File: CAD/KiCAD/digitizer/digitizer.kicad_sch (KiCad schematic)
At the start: 0 parts

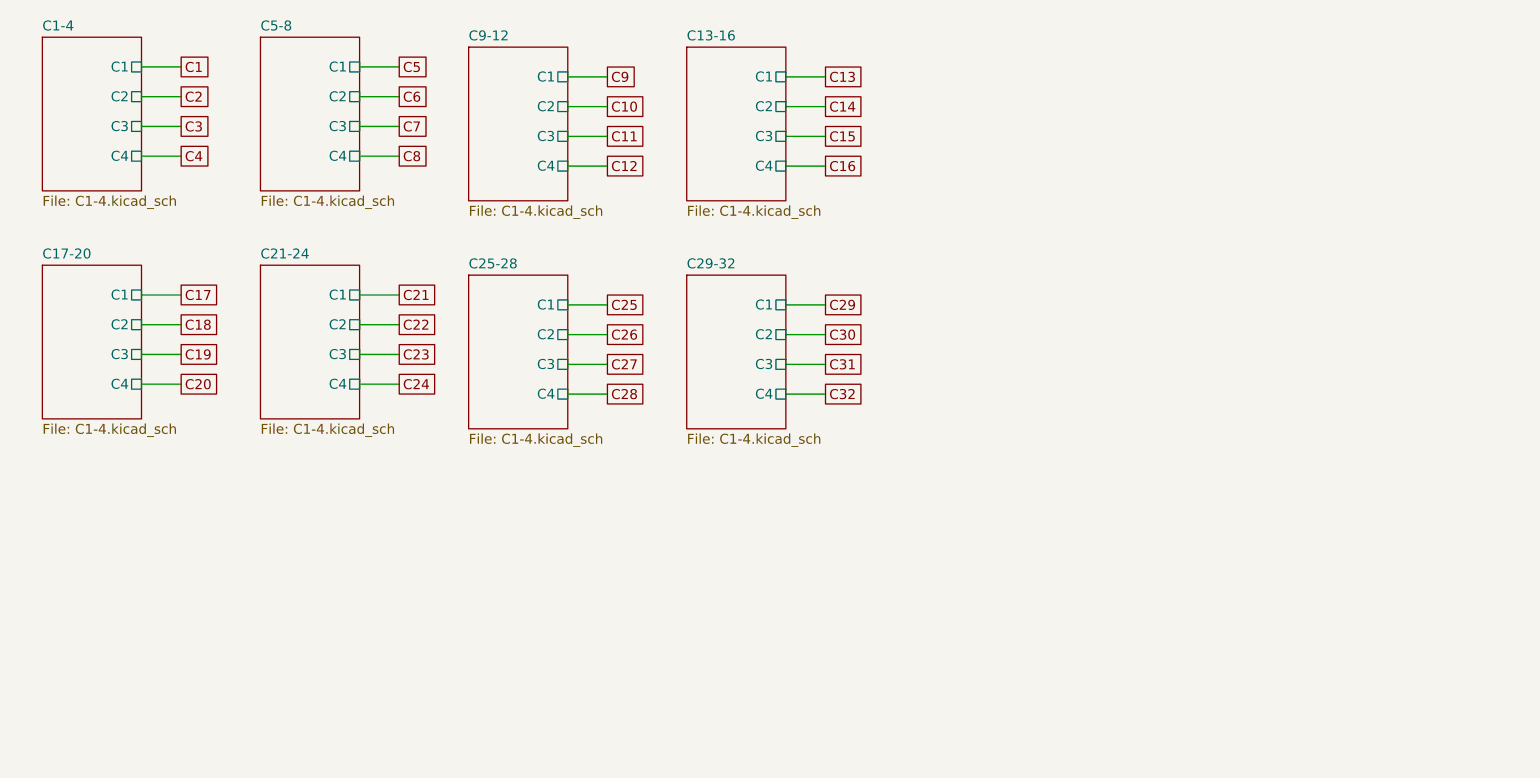
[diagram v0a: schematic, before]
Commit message: add MCP23017 for rows (no routing)
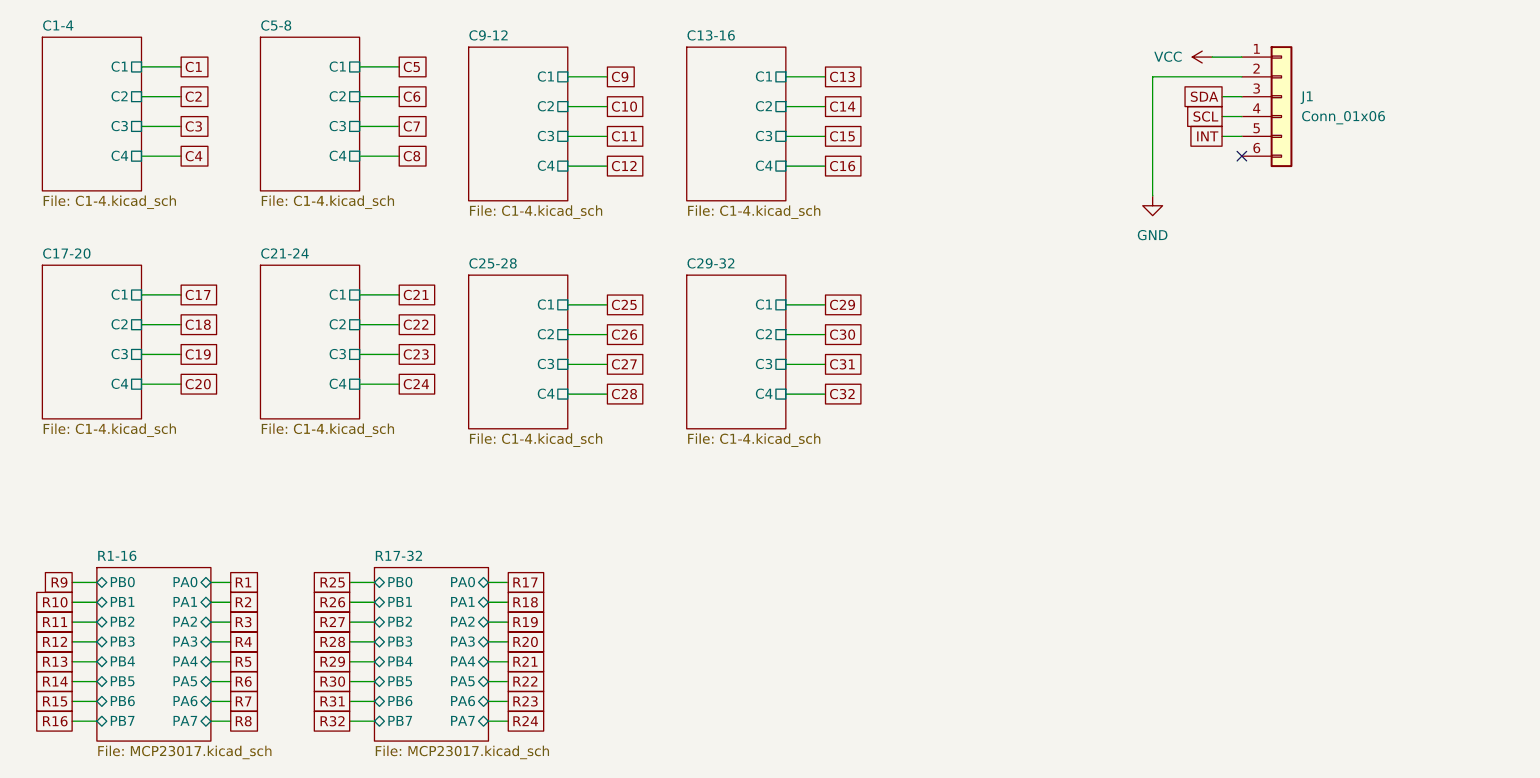
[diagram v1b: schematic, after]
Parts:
- added J1: Conn_01x06, Connector_PinHeader_2.54mm:PinHeader_1x06_P2.54mm_Vertical, symbol Connector_Generic:Conn_01x06
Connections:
- new net GND: J1.2 (Pin_2)
- new net INT: J1.5 (Pin_5)
- new net SCL: J1.4 (Pin_4)
- new net SDA: J1.3 (Pin_3)
- new net VCC: J1.1 (Pin_1)
- no-connect marks 0 -> 1
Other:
- added sheet R1-16 (MCP23017.kicad_sch)
- added sheet R17-32 (MCP23017.kicad_sch)

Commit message: one MCP23017 added and routed
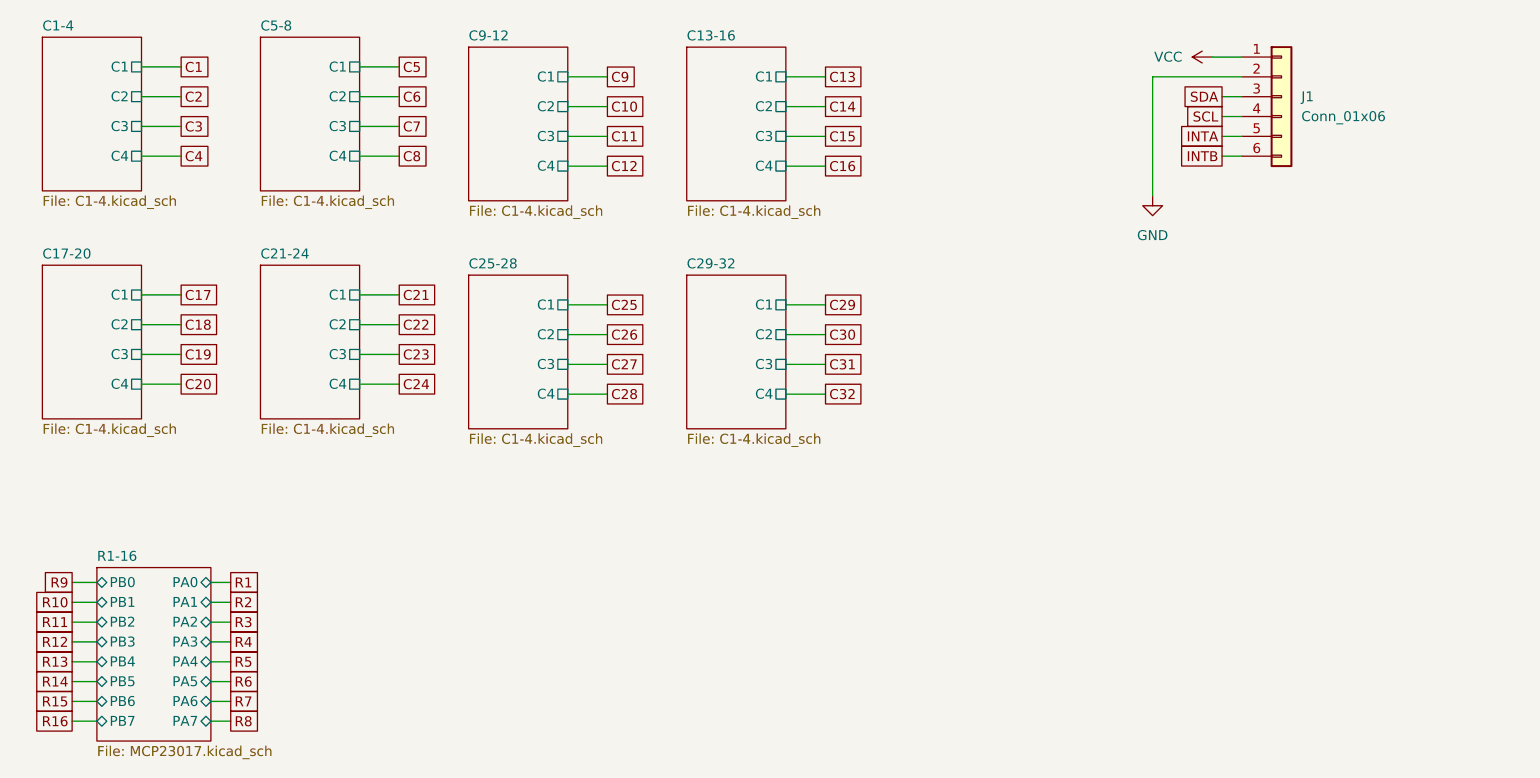
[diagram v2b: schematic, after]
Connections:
- net INTB: now reaches J1.6 (Pin_6)
- net INT renamed INTA
- no-connect marks 1 -> 0
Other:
- removed sheet R17-32

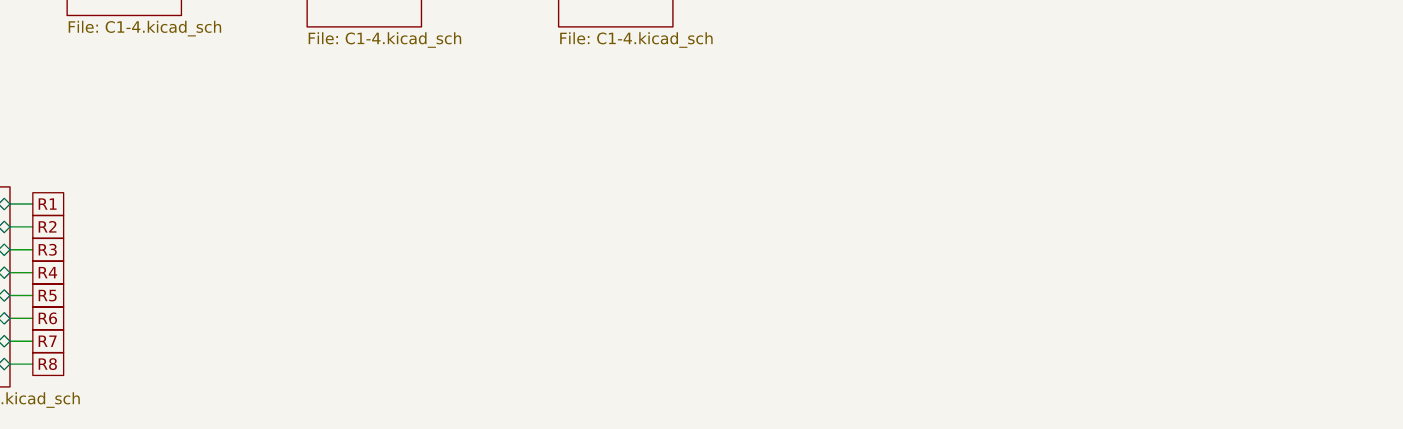
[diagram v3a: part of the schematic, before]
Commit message: digitizer draft with MCP23017 routing
Made-with: Cursor
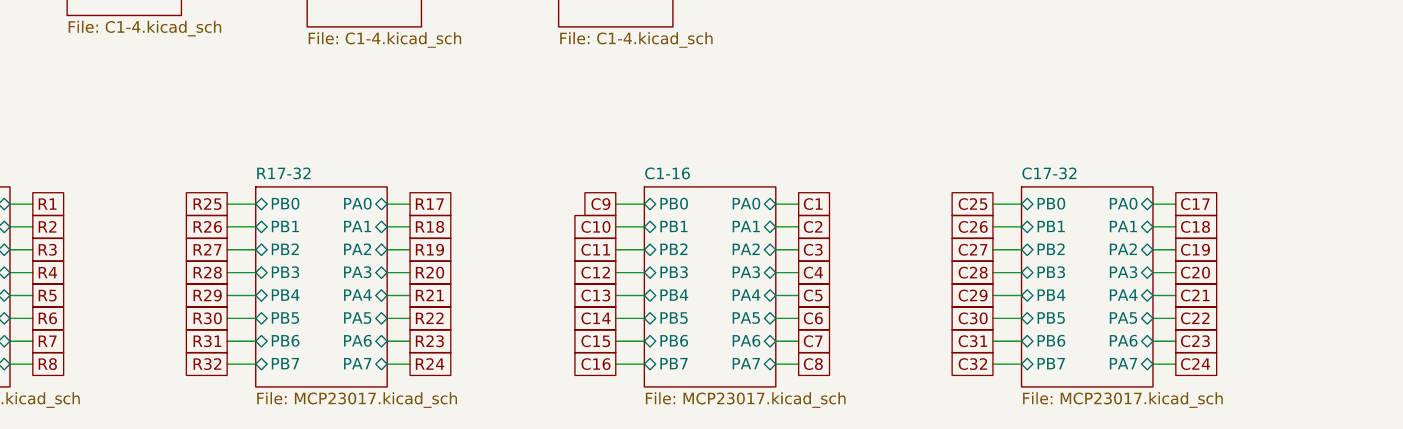
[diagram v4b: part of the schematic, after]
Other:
- added sheet C1-16 (MCP23017.kicad_sch)
- added sheet C17-32 (MCP23017.kicad_sch)
- added sheet R17-32 (MCP23017.kicad_sch)

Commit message: wip
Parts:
- added J2: Conn_01x06, Connector_PinHeader_2.54mm:PinHeader_1x06_P2.54mm_Vertical, symbol Connector_Generic:Conn_01x06
- added R1, R2: 10k, Resistor_THT:R_Axial_DIN0207_L6.3mm_D2.5mm_P15.24mm_Horizontal, symbol Device:R_US
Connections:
- net GND: now also J2.2 (Pin_2)
- net INTA: now also J2.5 (Pin_5)
- net INTB: now also J2.6 (Pin_6)
- net SCL: now also J2.4 (Pin_4), R2.2
- net SDA: now also J2.3 (Pin_3), R1.2
- net VCC: now also J2.1 (Pin_1), R1.1, R2.1

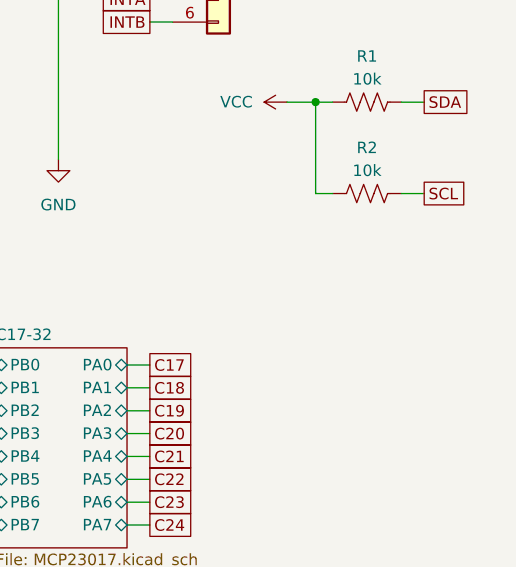
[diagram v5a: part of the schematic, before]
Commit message: cad: add pull-up resistors to interrupt lines
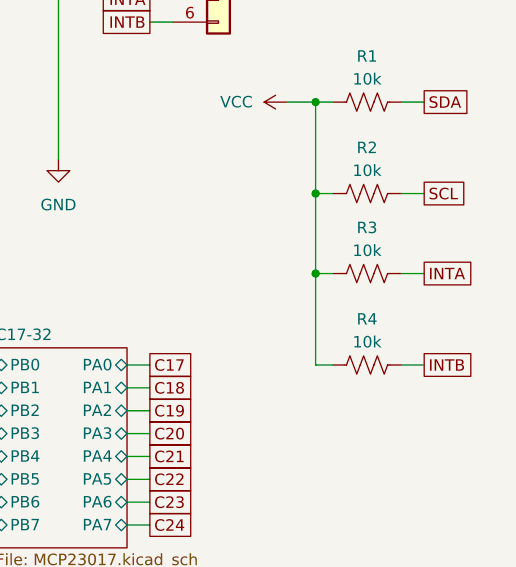
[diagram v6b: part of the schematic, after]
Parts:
- added R3, R4: 10k, Resistor_THT:R_Axial_DIN0207_L6.3mm_D2.5mm_P15.24mm_Horizontal, symbol Device:R_US
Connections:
- net INTA: now also R3.2
- net INTB: now also R4.2
- net VCC: now also R3.1, R4.1
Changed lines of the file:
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@@
 		(color 0 0 0 0)
 	)
+	(junction
+		(at 207.645 85.09)
+		(diameter 0)
+		(color 0 0 0 0)
+	)
+	(junction
+		(at 207.645 76.2)
+		(diameter 0)
+		(color 0 0 0 0)
+	)
 	(wire
 		(pts
@@
 	(wire
 		(pts
+			(xy 217.17 85.09) (xy 219.71 85.09)
+		)
+		(stroke
+			(width 0)
+			(type default)
+		)
+	)
+	(wire
+		(pts
 			(xy 50.8 40.64) (xy 55.88 40.64)
 		)
@@
 	(wire
 		(pts
+			(xy 207.645 85.09) (xy 207.645 95.25)
+		)
+		(stroke
+			(width 0)
+			(type default)
+		)
+	)
+	(wire
+		(pts
 			(xy 105.41 30.48) (xy 110.49 30.48)
 		)
@@
 	(wire
 		(pts
+			(xy 217.17 95.25) (xy 219.71 95.25)
+		)
+		(stroke
+			(width 0)
+			(type default)
+		)
+	)
+	(wire
+		(pts
 			(xy 189.23 52.07) (xy 191.77 52.07)
 		)
@@
 	(wire
 		(pts
+			(xy 209.55 85.09) (xy 207.645 85.09)
+		)
+		(stroke
+			(width 0)
+			(type default)
+		)
+	)
+	(wire
+		(pts
 			(xy 186.69 113.03) (xy 189.23 113.03)
 		)
@@
 	(wire
 		(pts
+			(xy 207.645 76.2) (xy 207.645 85.09)
+		)
+		(stroke
+			(width 0)
+			(type default)
+		)
+	)
+	(wire
+		(pts
 			(xy 133.35 34.29) (xy 138.43 34.29)
 		)
@@
 	(wire
 		(pts
+			(xy 209.55 95.25) (xy 207.645 95.25)
+		)
+		(stroke
+			(width 0)
+			(type default)
+		)
+	)
+	(wire
+		(pts
 			(xy 179.07 30.48) (xy 191.77 30.48)
 		)
@@
 		)
 	)
+	(global_label "INTB"
+		(shape passive)
+		(at 219.71 95.25 0)
+		(fields_autoplaced yes)
+		(effects
+			(font
+				(size 1.27 1.27)
+			)
+			(justify left)
+		)
+		(property "Intersheetrefs" "${INTERSHEET_REFS}"
+			(at 225.7568 95.25 0)
+			(effects
+				(font
+					(size 1.27 1.27)
+				)
+				(justify left)
+				(hide yes)
+			)
+		)
+	)
 	(global_label "C11"
 		(shape passive)
@@
 		)
 	)
+	(global_label "INTA"
+		(shape passive)
+		(at 219.71 85.09 0)
+		(fields_autoplaced yes)
+		(effects
+			(font
+				(size 1.27 1.27)
+			)
+			(justify left)
+		)
+		(property "Intersheetrefs" "${INTERSHEET_REFS}"
+			(at 225.5754 85.09 0)
+			(effects
+				(font
+					(size 1.27 1.27)
+				)
+				(justify left)
+				(hide yes)
+			)
+		)
+	)
 	(global_label "C26"
 		(shape passive)
@@
 	)
 	(symbol
+		(lib_id "Device:R_US")
+		(at 213.36 85.09 90)
+		(unit 1)
+		(exclude_from_sim no)
+		(in_bom yes)
+		(on_board yes)
+		(dnp no)
+		(property "Reference" "R3"
+			(at 213.36 80.01 90)
+			(effects
+				(font
+					(size 1.27 1.27)
+				)
+			)
+		)
+		(property "Value" "10k"
+			(at 213.36 82.55 90)
+			(effects
+				(font
+					(size 1.27 1.27)
+				)
+			)
+		)
+		(property "Footprint" "Resistor_THT:R_Axial_DIN0207_L6.3mm_D2.5mm_P15.24mm_Horizontal"
+			(at 213.614 84.074 90)
+			(effects
+				(font
+					(size 1.27 1.27)
+				)
+				(hide yes)
+			)
+		)
+		(property "Datasheet" "~"
+			(at 213.36 85.09 0)
+			(effects
+				(font
+					(size 1.27 1.27)
+				)
+				(hide yes)
+			)
+		)
+		(property "Description" "Resistor, US symbol"
+			(at 213.36 85.09 0)
+			(effects
+				(font
+					(size 1.27 1.27)
+				)
+				(hide yes)
+			)
+		)
+		(pin "2"
+		)
+		(pin "1"
+		)
+		(instances
+			(project "digitizer"
+				(path "/7204cdda-0a14-40c0-9dc8-8318dd514140"
+					(reference "R3")
+					(unit 1)
+				)
+			)
+		)
+	)
+	(symbol
 		(lib_id "power:VCC")
 		(at 176.53 27.94 90)
@@
 					(unit 1)
 				)
+			)
+		)
+	)
+	(symbol
+		(lib_id "Device:R_US")
+		(at 213.36 95.25 90)
+		(unit 1)
+		(exclude_from_sim no)
+		(in_bom yes)
+		(on_board yes)
+		(dnp no)
+		(property "Reference" "R4"
+			(at 213.36 90.17 90)
+			(effects
+				(font
+					(size 1.27 1.27)
+				)
+			)
+		)
+		(property "Value" "10k"
+			(at 213.36 92.71 90)
+			(effects
+				(font
+					(size 1.27 1.27)
+				)
+			)
+		)
+		(property "Footprint" "Resistor_THT:R_Axial_DIN0207_L6.3mm_D2.5mm_P15.24mm_Horizontal"
+			(at 213.614 94.234 90)
+			(effects
+				(font
+					(size 1.27 1.27)
+				)
+				(hide yes)
+			)
+		)
+		(property "Datasheet" "~"
+			(at 213.36 95.25 0)
+			(effects
+				(font
+					(size 1.27 1.27)
+				)
+				(hide yes)
+			)
+		)
+		(property "Description" "Resistor, US symbol"
+			(at 213.36 95.25 0)
+			(effects
+				(font
+					(size 1.27 1.27)
+				)
+				(hide yes)
+			)
+		)
+		(pin "2"
+		)
+		(pin "1"
+		)
+		(instances
+			(project "digitizer"
+				(path "/7204cdda-0a14-40c0-9dc8-8318dd514140"
+					(reference "R4")
+					(unit 1)
+				)
